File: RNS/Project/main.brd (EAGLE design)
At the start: 70.8 x 57.1 mm, 10 parts

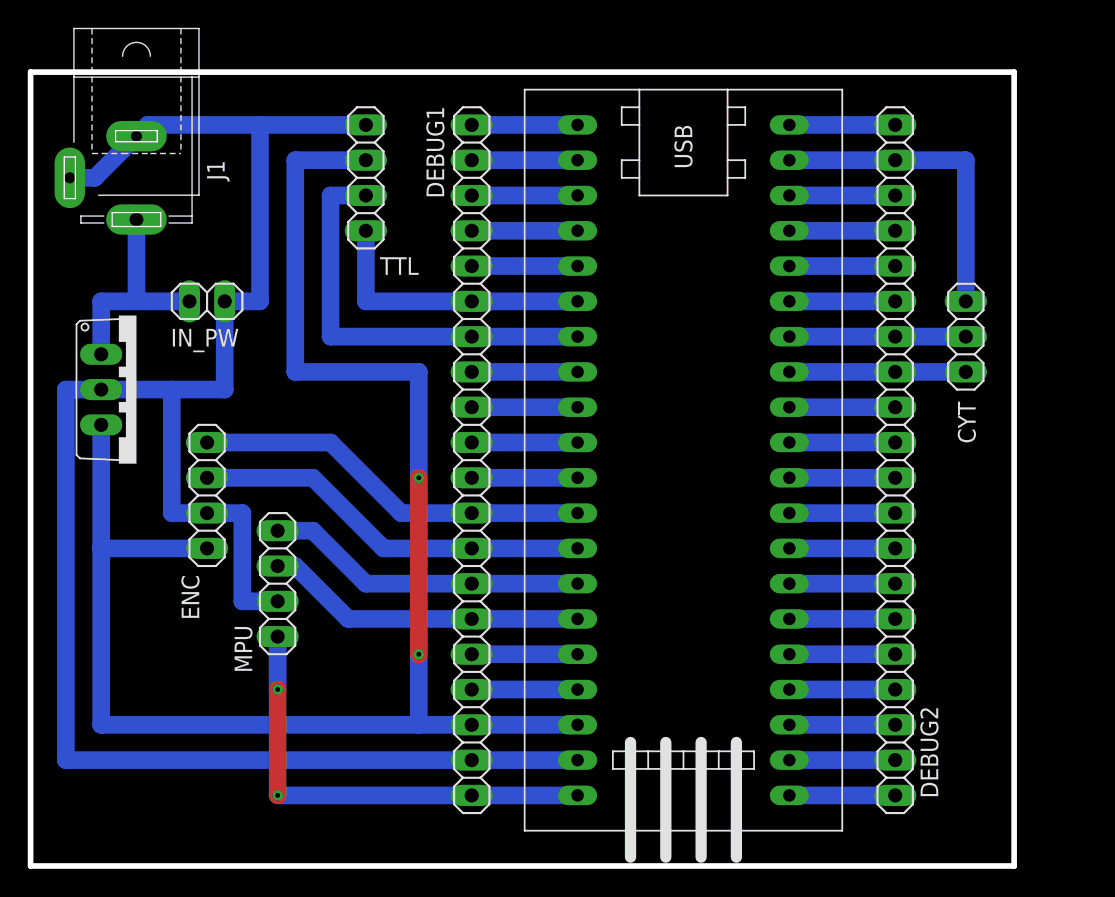
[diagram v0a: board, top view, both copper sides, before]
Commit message: Change design to fit IMU and Power Base inside the board
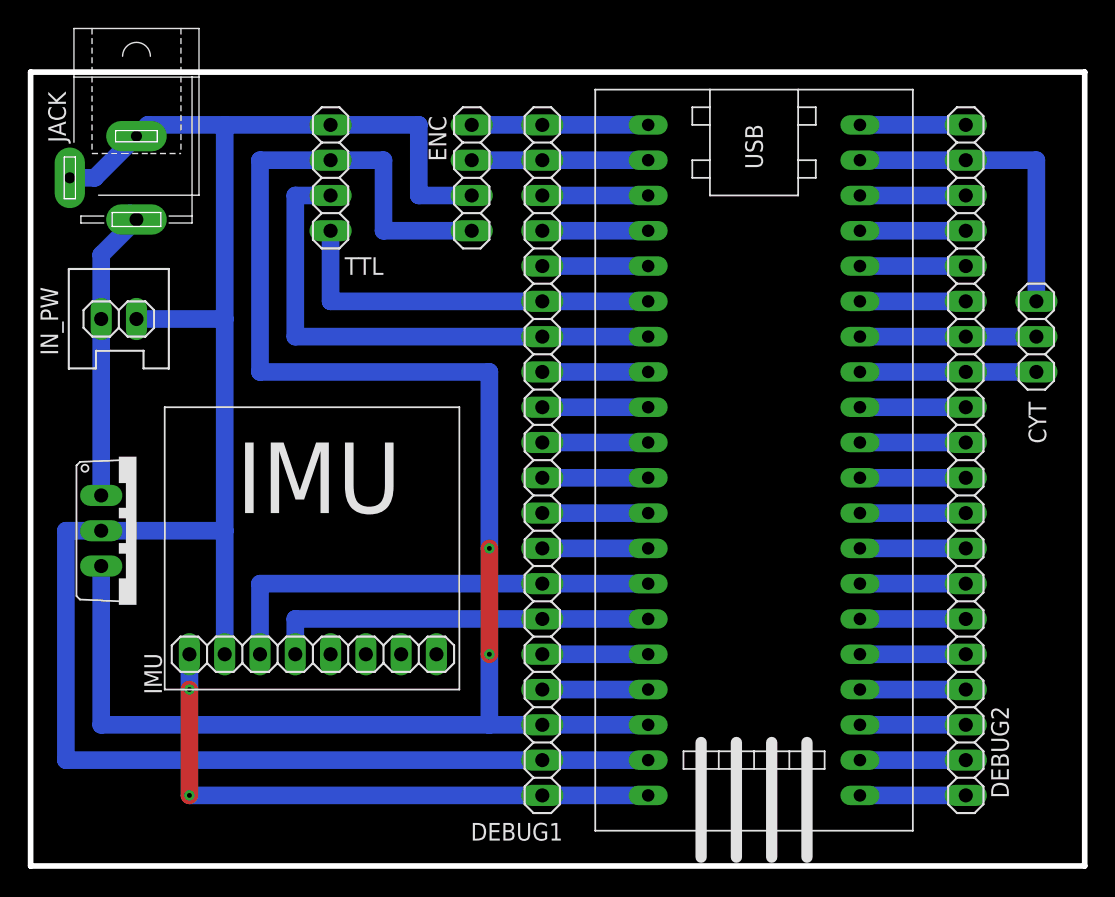
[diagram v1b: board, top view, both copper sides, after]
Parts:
- removed MPU: (no value), MIA-Training:1X04
- added IMU: IMU_ROBOCON_GY521, MIA_LIBRARY-2-2-2:IMU_GY521
- IN_PW: device MIA-Training:1X02 -> MIA_LIBRARY-2-2-2:1X02_DATA
- moved ENC 29.8 mm to (31.8, 49.5)
- moved REGULATOR 10.2 mm to (7.62, 24.1)
- moved IN_PW 6.48 mm to (6.35, 39.4)
- moved DEBUG2 5.08 mm to (67.3, 29.2)
- moved CYT 5.08 mm to (72.4, 38.1)
- moved DEBUG1 5.08 mm to (36.8, 29.2)
- moved STM 5.08 mm to (52.1, 30.5)
- moved TTL 2.54 mm to (21.6, 49.5)
- renumbered J1 to JACK
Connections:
- net 3.3V: now also IMU.VCC; no longer MPU.1
- net GND: now also IMU.GND; no longer MPU.2
- net PB_12: now also ENC.4
- net PB_13: now also ENC.3
- net PB_4: no longer ENC.4
- net PB_5: no longer ENC.3
- net PB_6: now also IMU.SCL; no longer MPU.4
- net PB_7: now also IMU.SDA; no longer MPU.3
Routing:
- net PB_5: track 28.8 -> 7.62 mm
- net PB_4: track 28.8 -> 7.62 mm
- net 5V: track 118.1 -> 128.3 mm
- net 3.3V: track 40.6 -> 50.8 mm
- net PB_6: track 23.2 -> 33.0 mm
- net PA_9: track 20.3 -> 27.9 mm
- net GND: track 172.7 -> 180.4 mm
- net PA_10: track 30.5 -> 38.1 mm
- net PB_13: track 7.62 -> 12.7 mm
- net PB_12: track 7.62 -> 12.7 mm
- net R_IN: track 16.7 -> 21.6 mm
- net PB_7: track 23.2 -> 27.9 mm
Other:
- board size 70.8 x 57.1 mm -> 75.9 x 57.1 mm
